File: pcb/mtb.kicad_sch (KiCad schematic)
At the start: 44 parts, among them J4 PINHEADER, J5 PROG/DEBUG, J6 PINHEADER, SW1 6x6, U12 STM32F103C8Tx, U13 AMS1117-3.3, U14 L78L05_SOT89, U15 SN75176AP, Y1 14,7456MHz

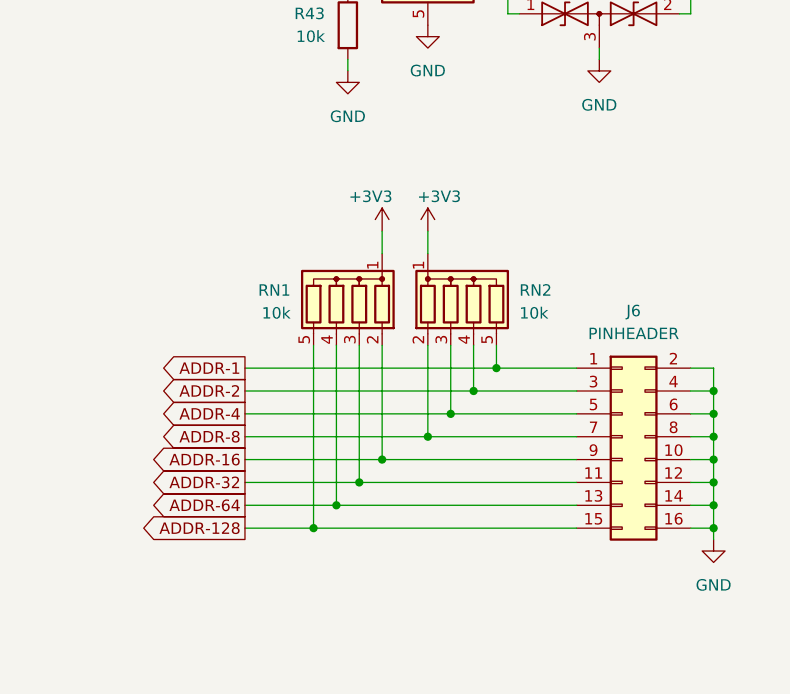
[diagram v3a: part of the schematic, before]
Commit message: Resistors added from 24.10.
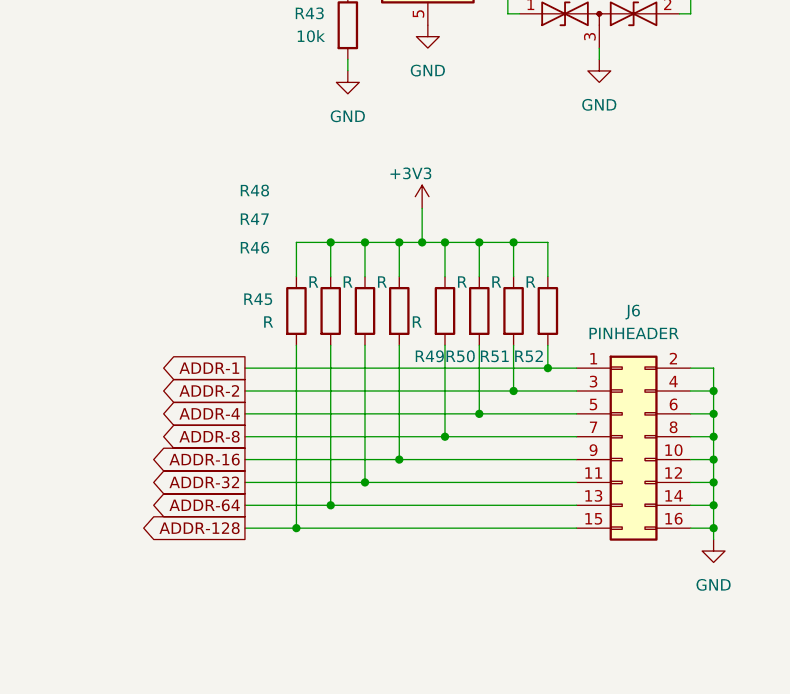
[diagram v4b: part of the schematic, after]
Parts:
- removed RN1, RN2: 10k, Resistor_THT:R_Array_SIP5, symbol Device:R_Network04
- added R45, R46, R47, R48, R49, R50, R51, R52: R, symbol Device:R
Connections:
- net +3V3: now also R45.1, R46.1, R47.1, R48.1, R49.1, R50.1, R51.1, R52.1
- net ADDR-1: now also R52.2
- net ADDR-128: now also R45.2
- net ADDR-16: now also R48.2
- net ADDR-2: now also R51.2
- net ADDR-32: now also R47.2
- net ADDR-4: now also R50.2
- net ADDR-64: now also R46.2
- net ADDR-8: now also R49.2

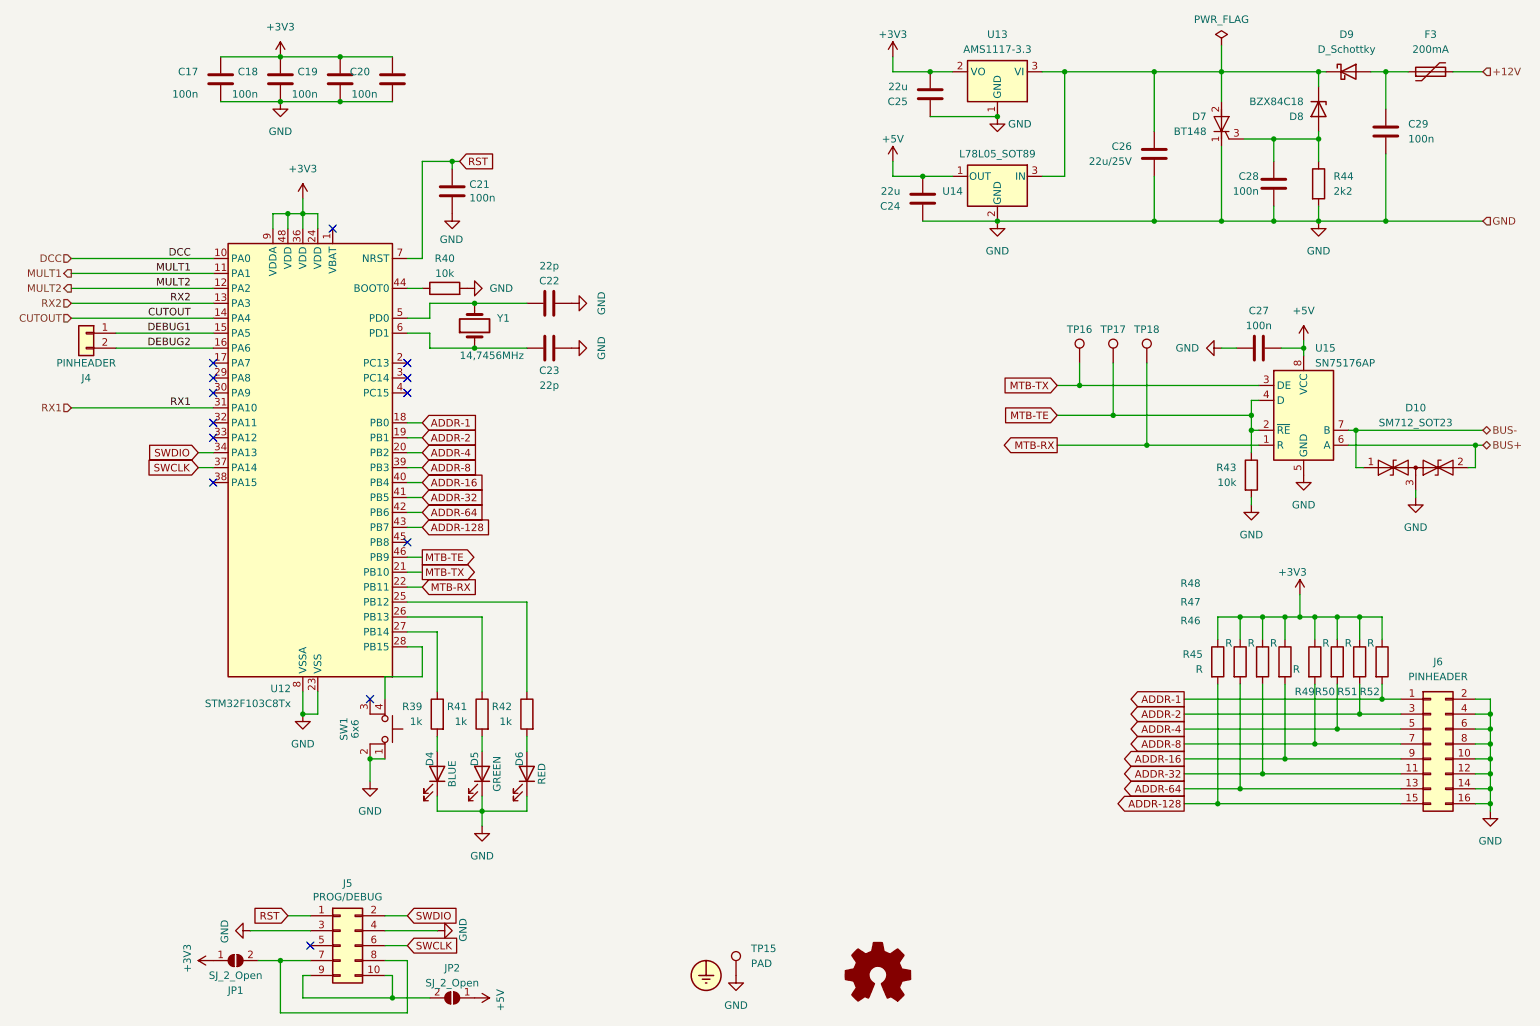
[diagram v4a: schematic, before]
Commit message: Added Sch.diodes, text editing..
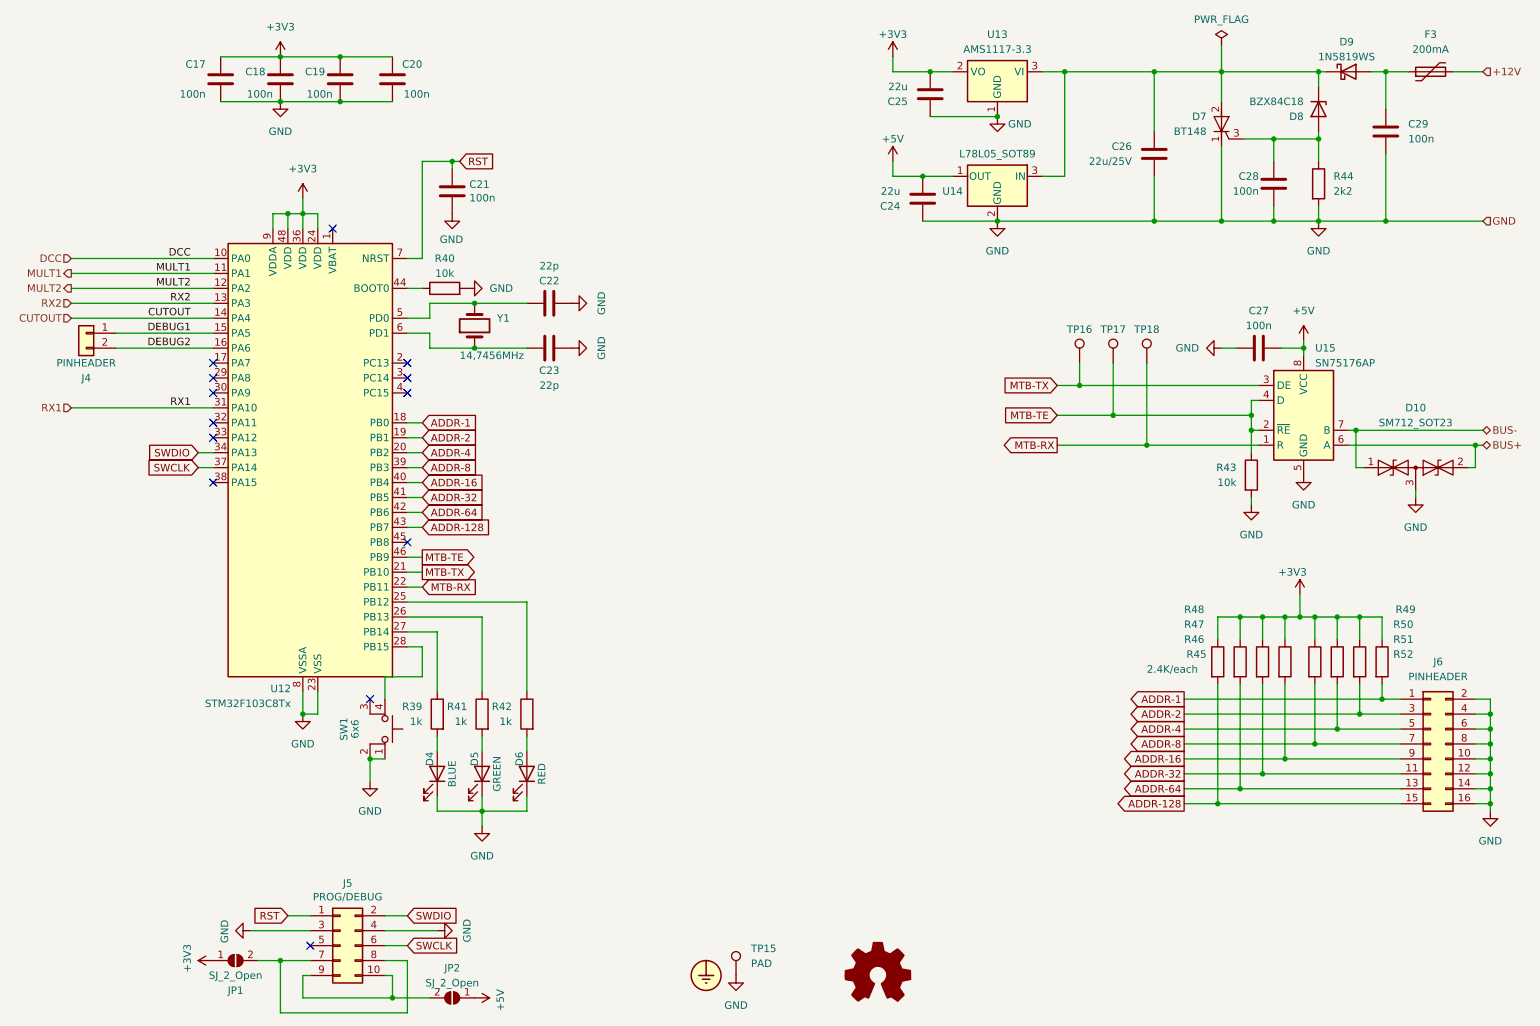
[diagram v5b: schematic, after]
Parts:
- removed D9: D_Schottky, symbol Device:D_Schottky
- added D9: 1N5819WS, Diode_SMD:D_SOD-123, symbol Diode:1N5819WS
- R45, R46, R47, R48, R49, R51, R52: value R -> 2.4k; footprint (none) -> Resistor_SMD:R_0805_2012Metric
- R50: value R -> 2.4K/each; footprint (none) -> Resistor_SMD:R_0805_2012Metric
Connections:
- net at C29.1, F3.1: now also D9.2 (A)
- net at C26.1, D7.2 (A), D8.3 (K)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: now also D9.1 (K)

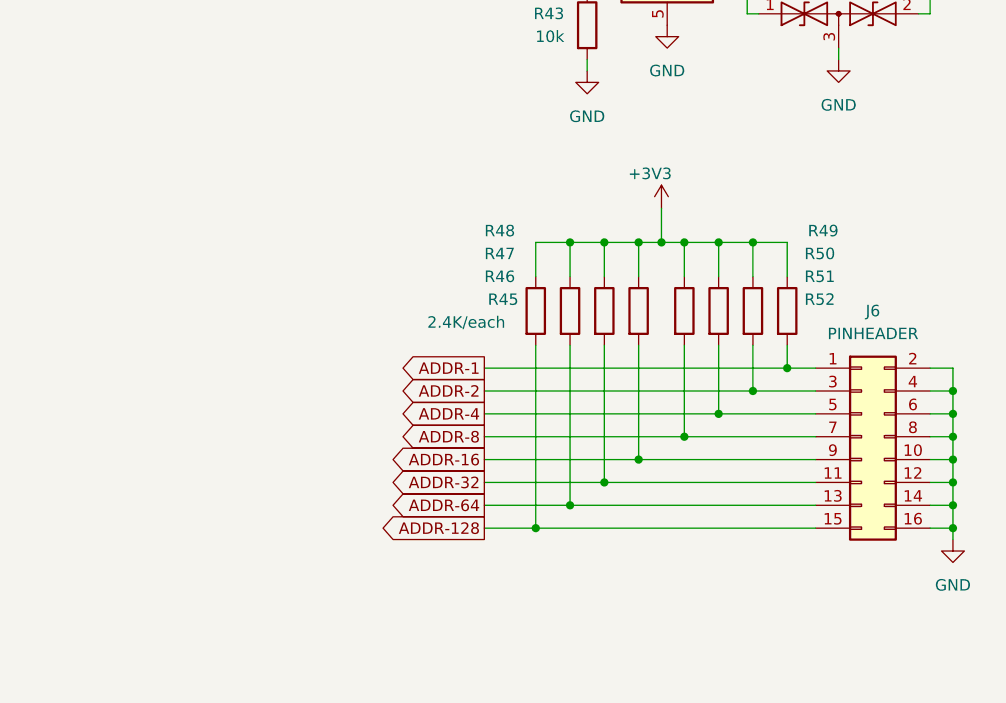
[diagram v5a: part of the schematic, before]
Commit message: Edited resistors in MTB part.
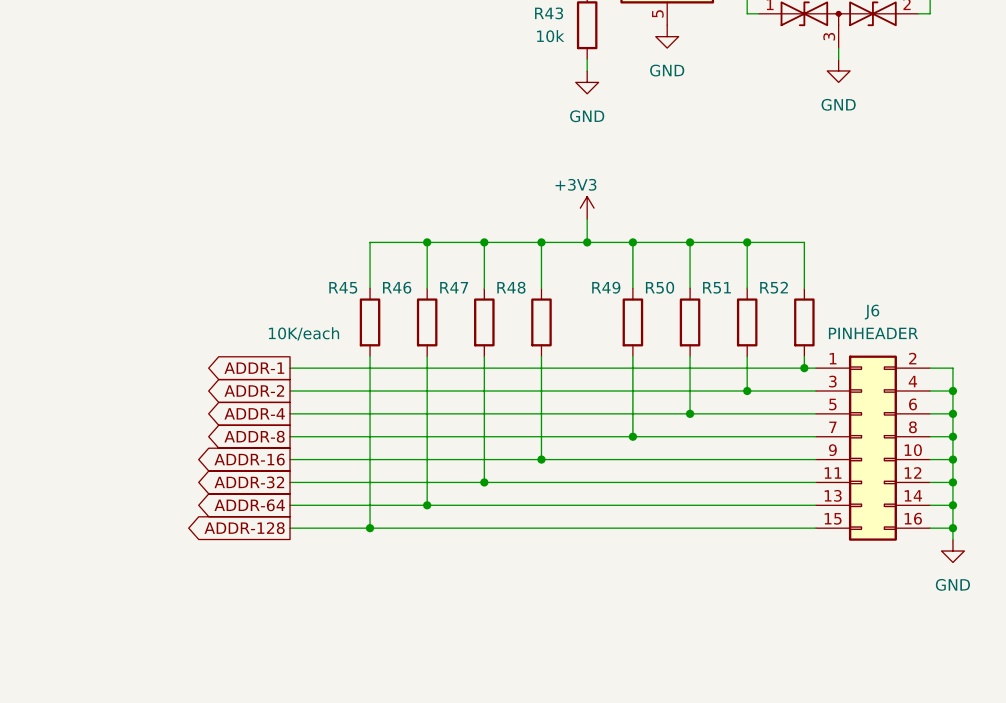
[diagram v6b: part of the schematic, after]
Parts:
- R50: value 2.4K/each -> 10K/each
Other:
- moved on the sheet: R45, R46, R47, R48, R49, R50, R51, R52

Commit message: Resistors values edited in mtb part.
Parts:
- R45, R46, R47, R48, R49, R52: value 2.4k -> 10k
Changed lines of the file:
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@@
       (effects (font (size 1.27 1.27)) (justify left))
     )
-    (property "Value" "2.4k" (at 251.46 126.365 0)
+    (property "Value" "10k" (at 251.46 126.365 0)
       (effects (font (size 1.27 1.27)) (justify left) hide)
     )
@@
       (effects (font (size 1.27 1.27)) (justify left))
     )
-    (property "Value" "2.4k" (at 222.25 126.365 0)
+    (property "Value" "10k" (at 222.25 126.365 0)
       (effects (font (size 1.27 1.27)) (justify left) hide)
     )
@@
       (effects (font (size 1.27 1.27)) (justify left))
     )
-    (property "Value" "2.4k" (at 215.9 126.365 0)
+    (property "Value" "10k" (at 215.9 126.365 0)
       (effects (font (size 1.27 1.27)) (justify left) hide)
     )
@@
       (effects (font (size 1.27 1.27)) (justify right))
     )
-    (property "Value" "2.4k" (at 203.2 130.81 0)
+    (property "Value" "10k" (at 203.2 130.81 0)
       (effects (font (size 1.27 1.27)) (justify right) hide)
     )
@@
       (effects (font (size 1.27 1.27)) (justify left))
     )
-    (property "Value" "2.4k" (at 209.55 126.365 0)
+    (property "Value" "10k" (at 209.55 126.365 0)
       (effects (font (size 1.27 1.27)) (justify left) hide)
     )
@@
       (effects (font (size 1.27 1.27)) (justify right))
     )
-    (property "Value" "2.4k" (at 232.41 130.81 0)
+    (property "Value" "10k" (at 232.41 130.81 0)
       (effects (font (size 1.27 1.27)) (justify right) hide)
     )

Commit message: eddited again.
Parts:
- R50: value 10K/each -> 10k
- R51: value 2.4k -> 10k
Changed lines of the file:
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@@
     (effects (font (size 1.27 1.27)) (justify right bottom))
+  )
+  (label "10k{slash}each" (at 194.31 130.81 0) (fields_autoplaced)
+    (effects (font (size 1.27 1.27)) (justify left bottom))
   )
   (label "MULT1" (at 49.53 62.23 180) (fields_autoplaced)
@@
       (effects (font (size 1.27 1.27)) (justify left))
     )
-    (property "Value" "2.4k" (at 245.11 126.365 0)
+    (property "Value" "10k" (at 245.11 126.365 0)
       (effects (font (size 1.27 1.27)) (justify left) hide)
     )
@@
       (effects (font (size 1.27 1.27)) (justify left))
     )
-    (property "Value" "10K/each" (at 194.31 130.81 0)
-      (effects (font (size 1.27 1.27)) (justify left))
+    (property "Value" "10k" (at 242.57 129.54 0)
+      (effects (font (size 1.27 1.27)) (justify left) hide)
     )
     (property "Footprint" "Resistor_SMD:R_0805_2012Metric" (at 239.522 129.54 90)
